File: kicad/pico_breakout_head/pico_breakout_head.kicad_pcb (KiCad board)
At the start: 2 copper layers, 39 x 66 mm, 18 parts, among them J1 HDR F 2.54MM 20-pin VERT, J2 HDR F 2.54MM 20-pin VERT, J3 JST B6B-PH-K-S, J4 HDR M 2.54MM 4p VERT, J5 JST B2B-XH-A, J6 HDR M 2.54MM 9p VERT, Q1 BSS123, U1 Pico

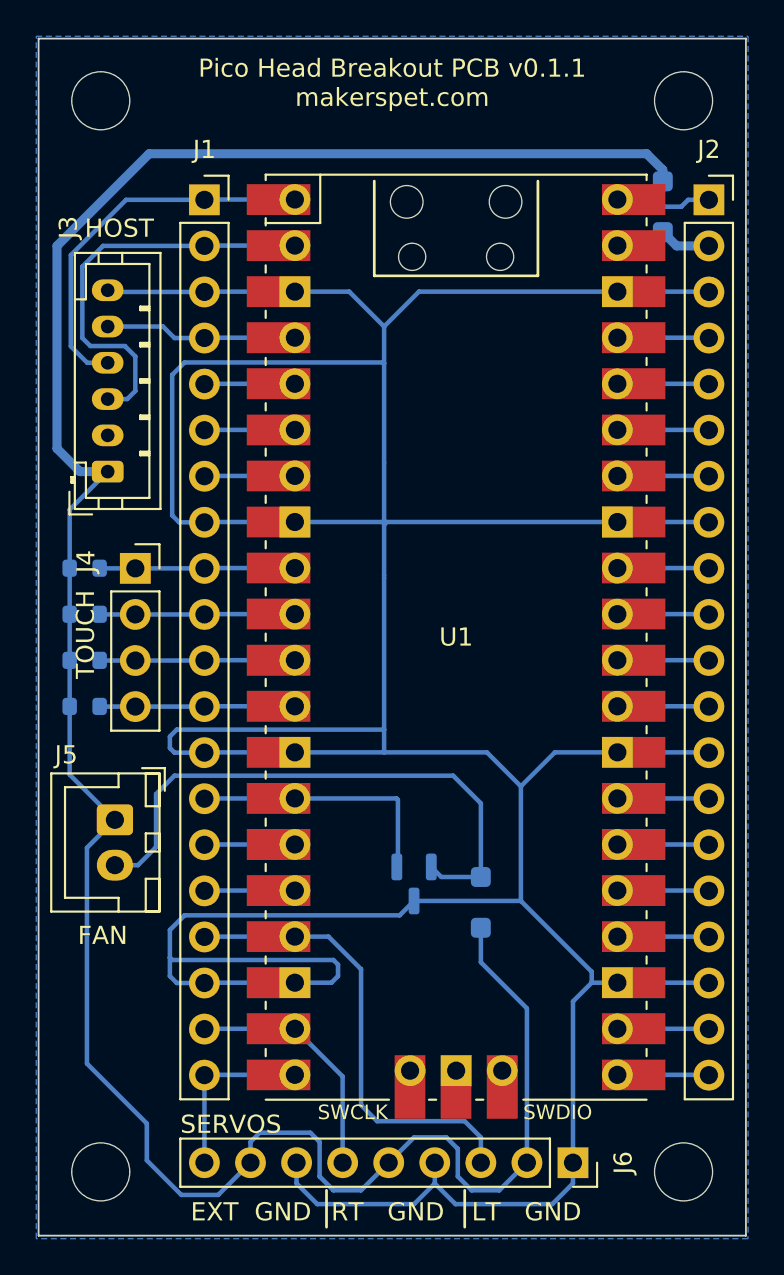
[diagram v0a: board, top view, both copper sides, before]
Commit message: Alt fuse; fan fix
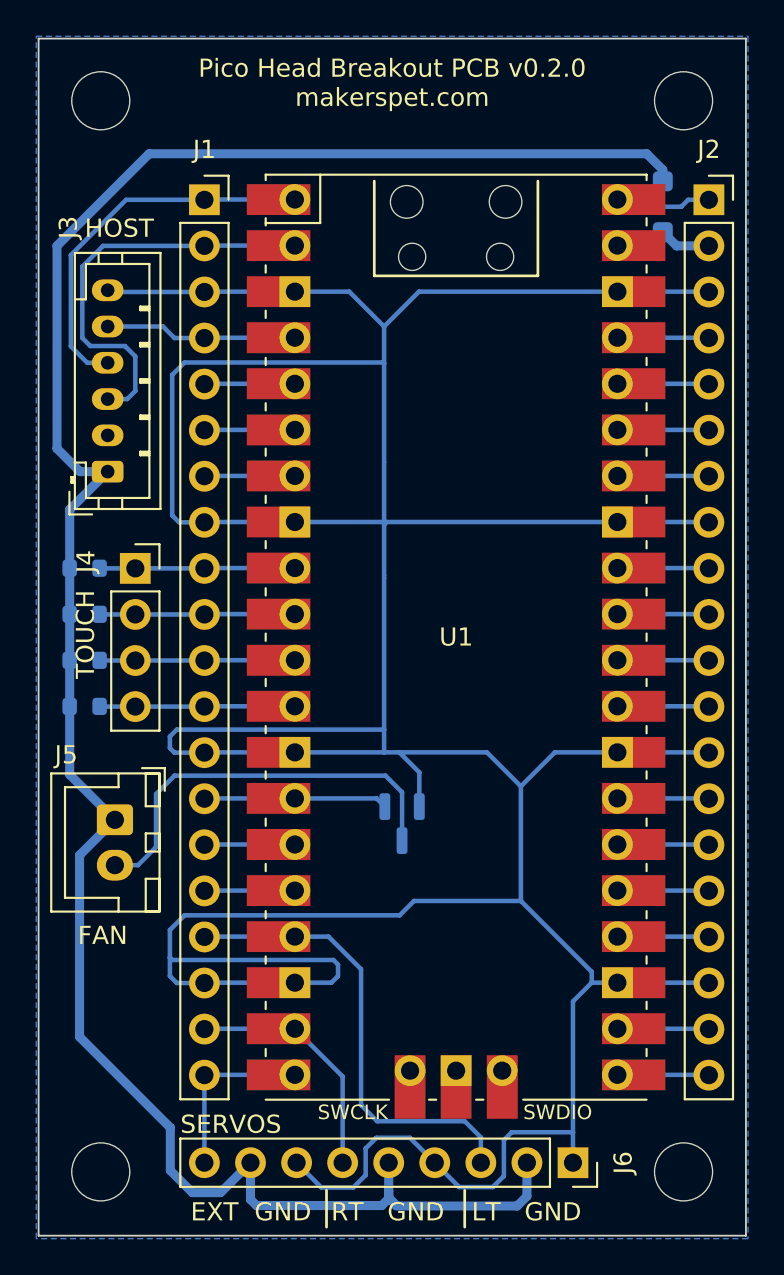
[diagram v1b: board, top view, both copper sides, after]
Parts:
- removed D1: FS26, Diode_SMD:D_SOD-123F
- Q1: value BSS123 -> AS2302
- moved Q1 3.39 mm to (158.3, 107.9)
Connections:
- J5 pad 2: Net-(D1-A) -> Net-(J5-Pin_2)
- Q1 pad 2: Net-(D1-A) -> GND
- Q1 pad 3: GND -> Net-(J5-Pin_2)
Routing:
- net Net-(D1-A): track 31.6 -> 0.00 mm
- net Net-(J5-Pin_2): track 0.00 -> 22.6 mm
- net +5V: track 137.1 -> 122.1 mm
- net /FAN_EN: track 14.4 -> 10.1 mm
- net GND: track 243.9 -> 248.1 mm
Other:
- board text added: "Pico Head Breakout PCB v0.2.0 makerspet.com"
- board text removed: "Pico Head Breakout PCB v0.1.1 makerspet.com"
